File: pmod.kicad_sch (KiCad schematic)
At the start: 2 parts, among them J5 PinSocket_2x6_P2.54mm_Drill1.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, J6 PinSocket_2x6_P2.54mm_Drill1.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

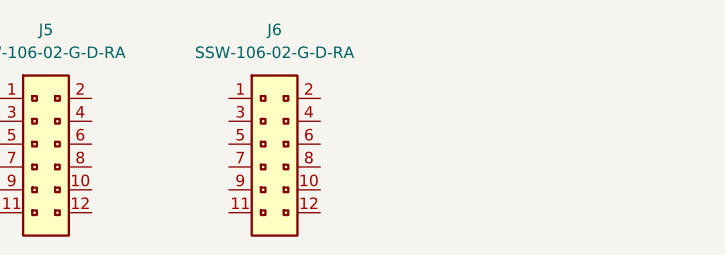
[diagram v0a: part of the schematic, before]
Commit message: [#94684] Add ports to subsheets
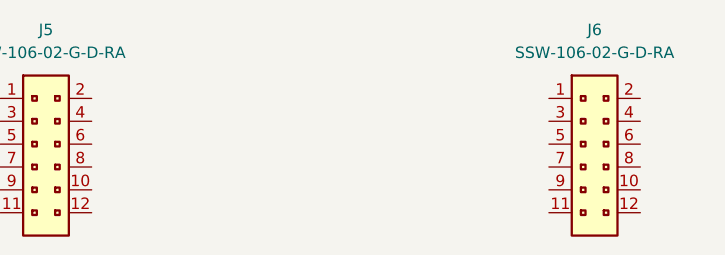
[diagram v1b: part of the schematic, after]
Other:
- moved on the sheet: J6
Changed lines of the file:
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@@
 	(generator "eeschema")
 	(generator_version "9.0")
-	(paper "A4")
+	(paper "A3")
 	(title_block
 		(title "renode-reference-platform")
@@
 	(symbol
 		(lib_id "antmicroGenericPinSockets:PinSocket_2x6_P2.54mm_Drill1.04mm_Horizontal")
-		(at 146.05 86.36 0)
+		(at 181.61 86.36 0)
 		(unit 1)
 		(exclude_from_sim no)
@@
 		(fields_autoplaced yes)
 		(property "Reference" "J6"
-			(at 151.13 78.74 0)
+			(at 186.69 78.74 0)
 			(effects
 				(font
@@
 		)
 		(property "Value" "PinSocket_2x6_P2.54mm_Drill1.04mm_Horizontal"
-			(at 165.1 88.9 0)
+			(at 200.66 88.9 0)
 			(effects
 				(font
@@
 		)
 		(property "Footprint" "antmicro-footprints:PinSocket_2x6_P2.54mm_Drill1.04mm_Horizontal"
-			(at 165.1 91.44 0)
+			(at 200.66 91.44 0)
 			(effects
 				(font
@@
 		)
 		(property "Datasheet" "https://suddendocs.samtec.com/prints/ssw-1xx-xx-xxx-x-xx-xxx-xx-mkt.pdf"
-			(at 165.1 93.98 0)
+			(at 200.66 93.98 0)
 			(effects
 				(font
@@
 		)
 		(property "Description" "PCB Receptacle, Board-to-Board, 2.54 mm, 2 Rows, 12 Contacts, Through Hole Mount Right Angle, SSW"
-			(at 165.1 106.68 0)
+			(at 200.66 106.68 0)
 			(effects
 				(font
@@
 		)
 		(property "MPN" "SSW-106-02-G-D-RA"
-			(at 151.13 81.28 0)
+			(at 186.69 81.28 0)
 			(effects
 				(font
@@
 		)
 		(property "Manufacturer" "Samtec"
-			(at 165.1 96.52 0)
+			(at 200.66 96.52 0)
 			(effects
 				(font
@@
 		)
 		(property "Author" "Antmicro"
-			(at 165.1 101.6 0)
+			(at 200.66 101.6 0)
 			(effects
 				(font
@@
 		)
 		(property "License" "Apache-2.0"
-			(at 165.1 104.14 0)
-			(effects
-				(font
+			(at 200.66 104.14 0)
+			(effects
+				(font

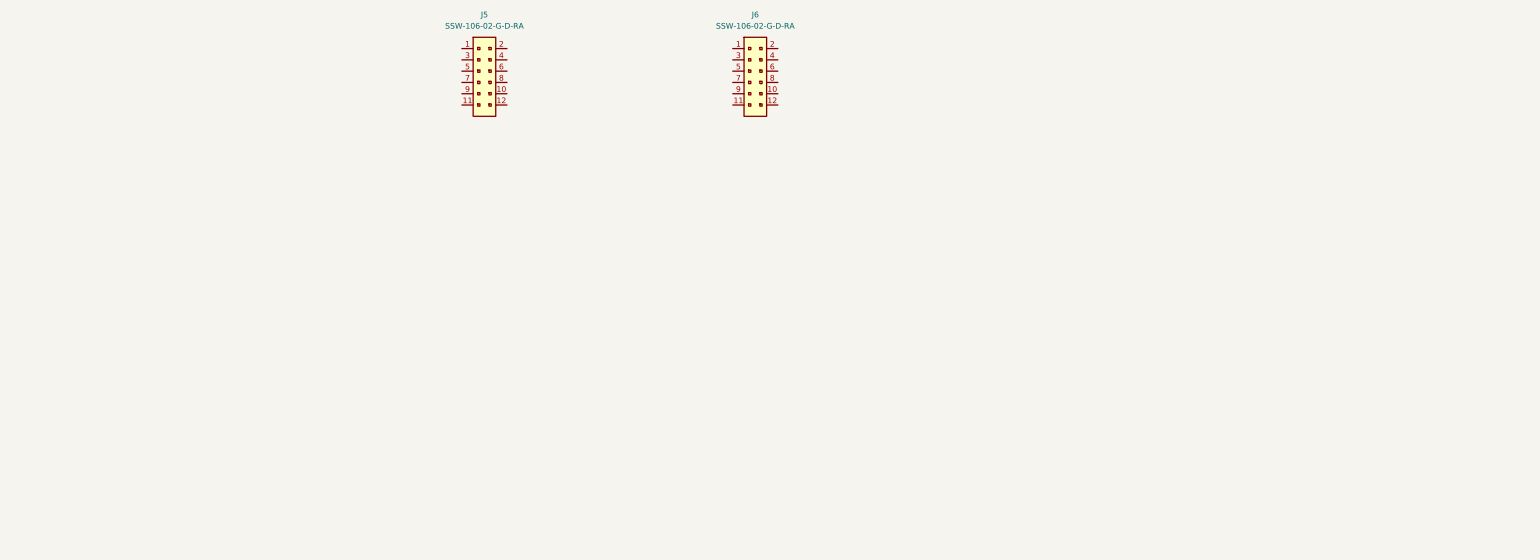
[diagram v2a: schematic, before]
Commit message: [#94862] Add PMOD interfaces
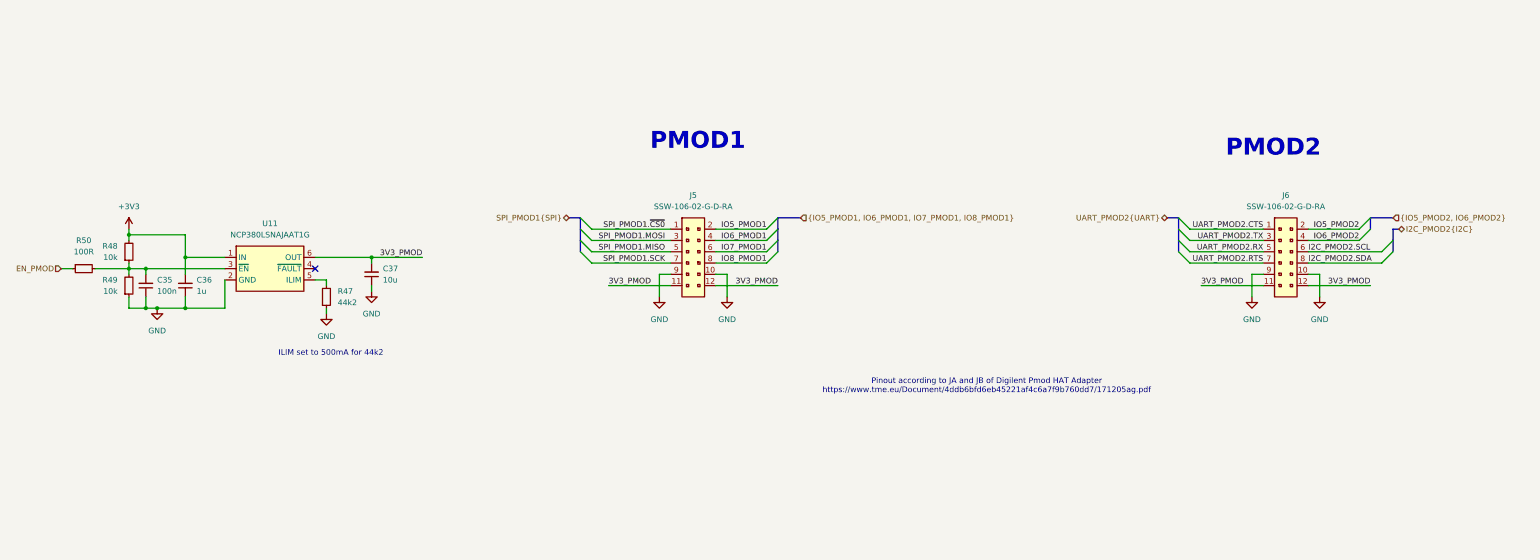
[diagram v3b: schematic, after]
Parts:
- added C35: C_100n_0402, antmicro-footprints:C_0402_1005Metric, symbol antmicroCapacitors0402:C_100n_0402
- added C36: C_1u_0402, antmicro-footprints:C_0402_1005Metric, symbol antmicroCapacitors0402:C_1u_0402
- added C37: C_10u_0402, antmicro-footprints:C_0402_1005Metric, symbol antmicroCapacitors0402:C_10u_0402
- added R47: R_44k2_0402, antmicro-footprints:R_0402_1005Metric, symbol antmicroResistors0402:R_44k2_0402
- added R48, R49: R_10k_0402, antmicro-footprints:R_0402_1005Metric, symbol antmicroResistors0402:R_10k_0402
- added R50: R_100R_0402, antmicro-footprints:R_0402_1005Metric, symbol antmicroResistors0402:R_100R_0402
- added U11: NCP380LSNAJAAT1G, antmicro-footprints:SOT-23-6, symbol antmicroPMICPowerDistributionSwitchesLoadDrivers:NCP380LSNAJAAT1G
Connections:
- net SPI_PMOD1.~{CS0}: now reaches J5.1
- net GND: now reaches J5.10
- net GND: now also J5.9, J6.10, J6.9, C35.1, C36.1, C37.1, R47.1, R49.1, U11.2 (GND)
- net 3V3_PMOD: now reaches J5.11
- net 3V3_PMOD: now also J5.12, J6.11, J6.12, C37.2, U11.6 (OUT)
- net IO5_PMOD1: now reaches J5.2
- net SPI_PMOD1.MOSI: now reaches J5.3
- net IO6_PMOD1: now reaches J5.4
- net SPI_PMOD1.MISO: now reaches J5.5
- net IO7_PMOD1: now reaches J5.6
- net SPI_PMOD1.SCK: now reaches J5.7
- net IO8_PMOD1: now reaches J5.8
- net UART_PMOD2.CTS: now reaches J6.1
- net IO5_PMOD2: now reaches J6.2
- net UART_PMOD2.TX: now reaches J6.3
- net IO6_PMOD2: now reaches J6.4
- net UART_PMOD2.RX: now reaches J6.5
- net I2C_PMOD2.SCL: now reaches J6.6
- net UART_PMOD2.RTS: now reaches J6.7
- net I2C_PMOD2.SDA: now reaches J6.8
- new net: C35.2, R48.1, R49.2, R50.2, U11.3 (~{EN})
- new net: R47.2, U11.5 (ILIM)
- new net +3V3: C36.2, R48.2, U11.1 (IN)
- new net EN_PMOD: R50.1
- no-connect marks 0 -> 1
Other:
- note added: "ILIM set to 500mA for 44k2"
- note added: "PMOD1"
- note added: "PMOD2"
- note added: "Pinout according to JA and JB of Digilent Pmod HAT Adapter https://www.tme.eu/Document/4ddb6bfd6eb45221af4c6a7f9b760dd7/171205ag.pdf"
- moved on the sheet: J5, J6

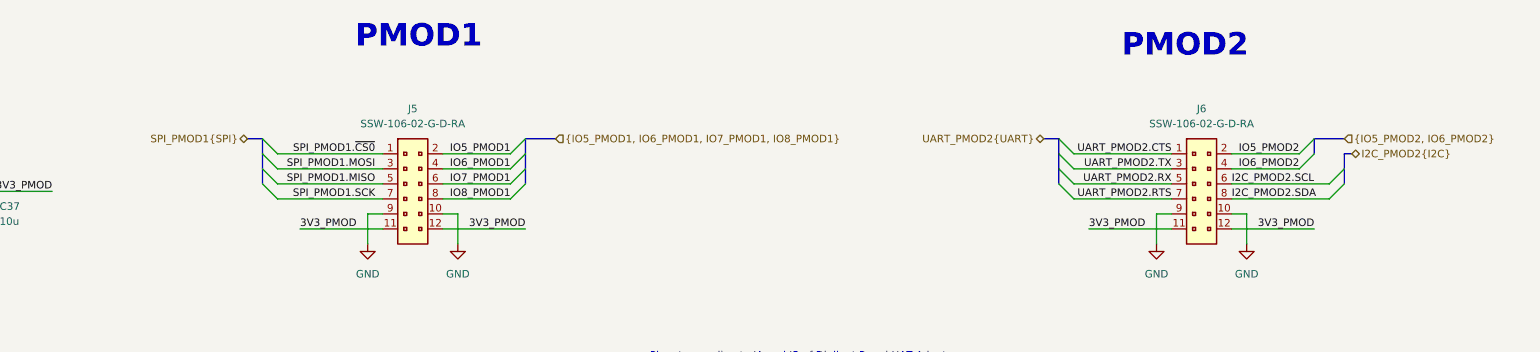
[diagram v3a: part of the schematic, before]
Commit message: [#95036] Rename PMOD signals
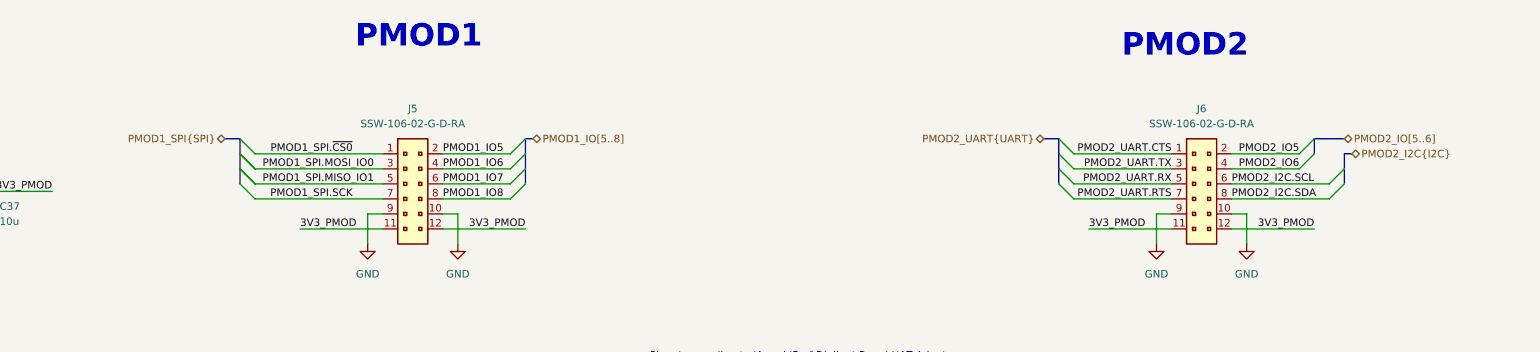
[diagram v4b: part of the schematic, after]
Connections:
- net I2C_PMOD2.SCL renamed PMOD2_I2C.SCL
- net I2C_PMOD2.SDA renamed PMOD2_I2C.SDA
- net IO5_PMOD1 renamed PMOD1_IO5
- net IO5_PMOD2 renamed PMOD2_IO5
- net IO6_PMOD1 renamed PMOD1_IO6
- net IO6_PMOD2 renamed PMOD2_IO6
- net IO7_PMOD1 renamed PMOD1_IO7
- net IO8_PMOD1 renamed PMOD1_IO8
- net SPI_PMOD1.MISO renamed PMOD1_SPI.MISO_IO1
- net SPI_PMOD1.MOSI renamed PMOD1_SPI.MOSI_IO0
- net SPI_PMOD1.SCK renamed PMOD1_SPI.SCK
- net SPI_PMOD1.~{CS0} renamed PMOD1_SPI.~{CS0}
- net UART_PMOD2.CTS renamed PMOD2_UART.CTS
- net UART_PMOD2.RTS renamed PMOD2_UART.RTS
- net UART_PMOD2.RX renamed PMOD2_UART.RX
- net UART_PMOD2.TX renamed PMOD2_UART.TX

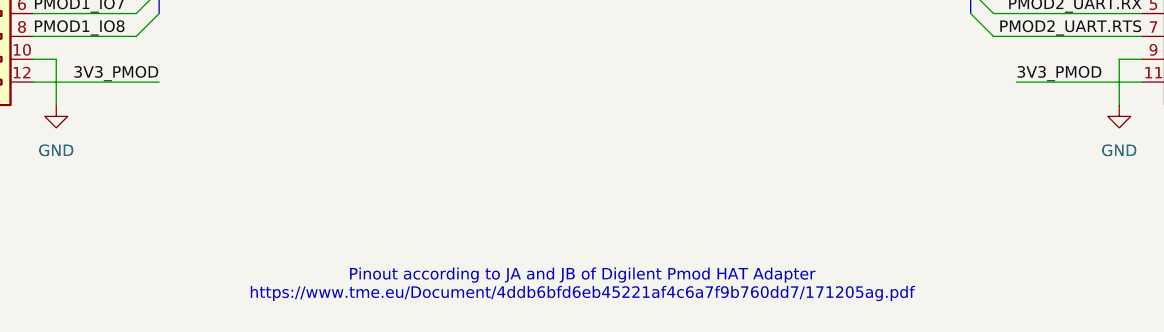
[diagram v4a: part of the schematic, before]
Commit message: [#95036] Connect PMOD pins to MCU
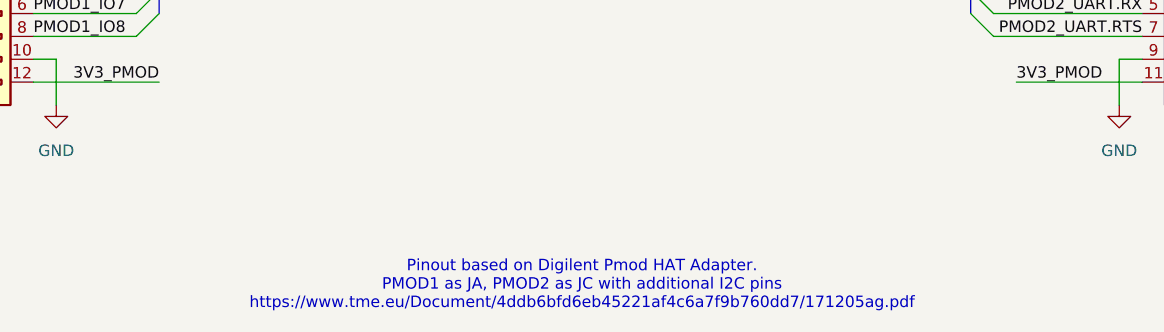
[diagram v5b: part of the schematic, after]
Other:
- note added: "Pinout based on Digilent Pmod HAT Adapter. PMOD1 as JA, PMOD2 as JC with additional I2C pins https://www.tme.eu/Document/4ddb6bfd6eb45221af4c6a7f9b760dd7/171205ag.pdf"
- note removed: "Pinout according to JA and JB of Digilent Pmod HAT Adapter https://www.tme.eu/Document/4ddb6bfd6eb45221af4c6a7f9b760dd7/171205ag.pdf"
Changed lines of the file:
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@@
 		(company "Antmicro")
 	)
-	(text "Pinout according to JA and JB of Digilent Pmod HAT Adapter\nhttps://www.tme.eu/Document/4ddb6bfd6eb45221af4c6a7f9b760dd7/171205ag.pdf"
+	(text "Pinout based on Digilent Pmod HAT Adapter.\nPMOD1 as JA, PMOD2 as JC with additional I2C pins \nhttps://www.tme.eu/Document/4ddb6bfd6eb45221af4c6a7f9b760dd7/171205ag.pdf"
 		(exclude_from_sim no)
 		(at 238.76 162.306 0)

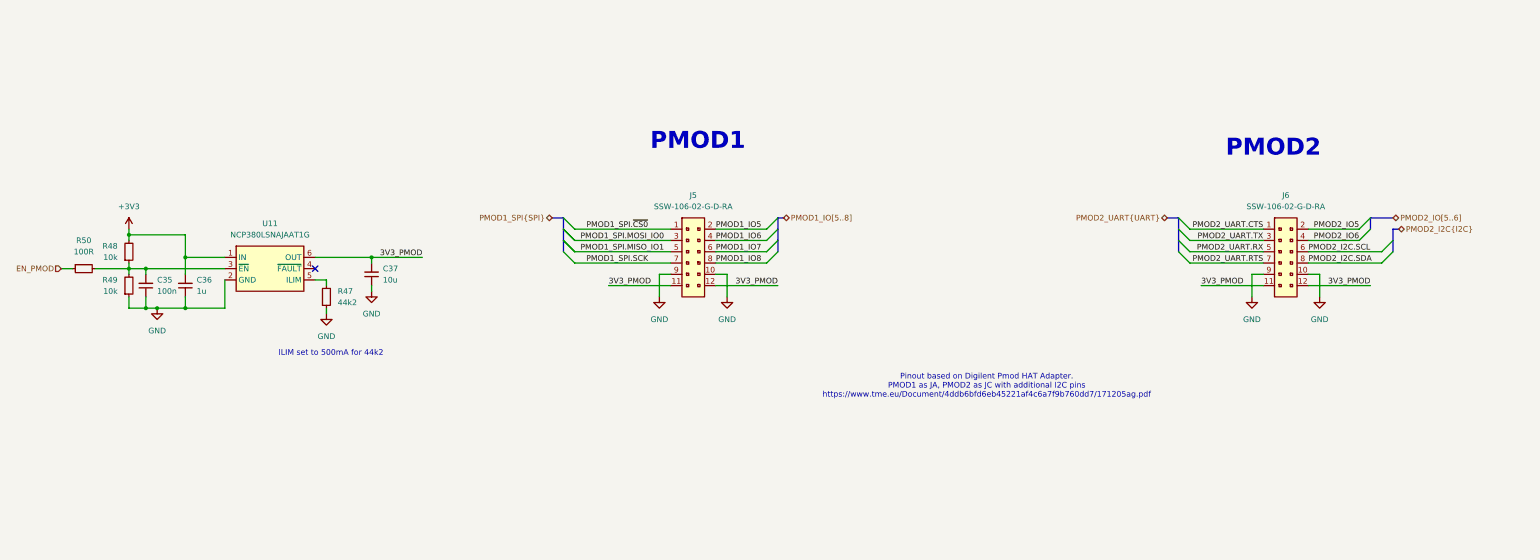
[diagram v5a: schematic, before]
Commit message: [#95036] Add schematic markings
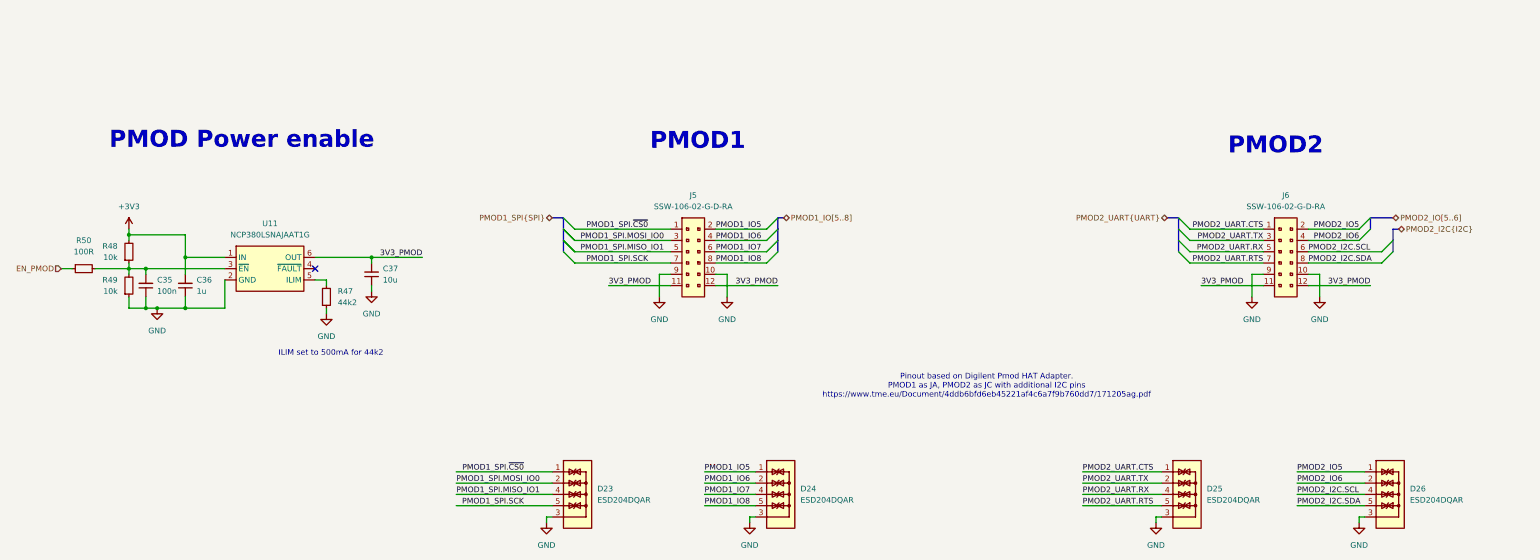
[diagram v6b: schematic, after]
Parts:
- added D23, D24, D25, D26: ESD204DQAR, antmicro-footprints:USON-10_2.5x1mm_P0.5mm, symbol antmicroTVSDiodes:ESD204DQAR
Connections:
- net GND: now also D23.3, D23.8, D24.3, D24.8, D25.3, D25.8, D26.3, D26.8
- net PMOD1_IO5: now also D24.1, D24.10
- net PMOD1_IO6: now also D24.2, D24.9
- net PMOD1_IO7: now also D24.4, D24.7
- net PMOD1_IO8: now also D24.5, D24.6
- net PMOD1_SPI.MISO_IO1: now also D23.4, D23.7
- net PMOD1_SPI.MOSI_IO0: now also D23.2, D23.9
- net PMOD1_SPI.SCK: now also D23.5, D23.6
- net PMOD1_SPI.~{CS0}: now also D23.1, D23.10
- net PMOD2_I2C.SCL: now also D26.4, D26.7
- net PMOD2_I2C.SDA: now also D26.5, D26.6
- net PMOD2_IO5: now also D26.1, D26.10
- net PMOD2_IO6: now also D26.2, D26.9
- net PMOD2_UART.CTS: now also D25.1, D25.10
- net PMOD2_UART.RTS: now also D25.5, D25.6
- net PMOD2_UART.RX: now also D25.4, D25.7
- net PMOD2_UART.TX: now also D25.2, D25.9
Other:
- note added: "PMOD Power enable"

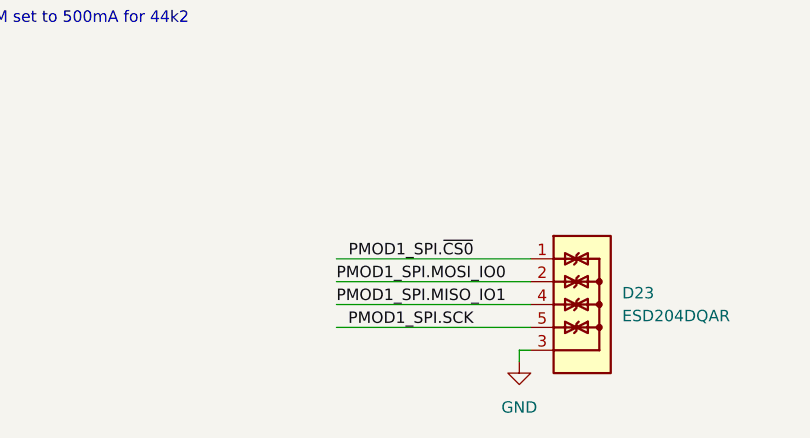
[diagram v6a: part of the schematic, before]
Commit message: [#95036] Solve ERC
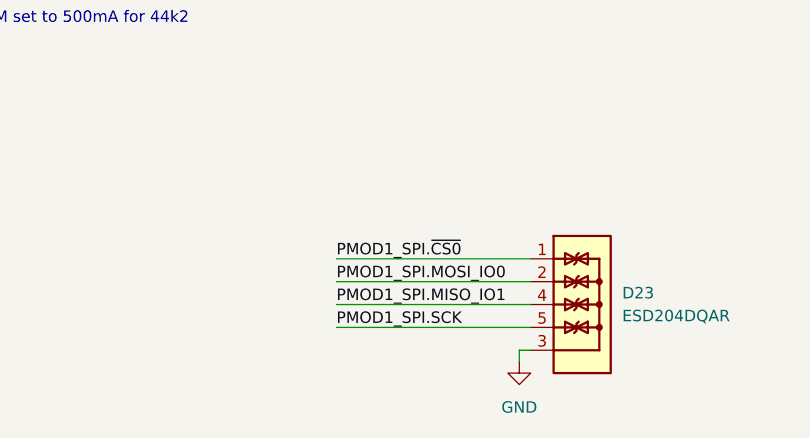
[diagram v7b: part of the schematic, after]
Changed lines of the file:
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@@
 	)
 	(label "PMOD1_SPI.SCK"
-		(at 134.62 189.23 180)
-		(effects
-			(font
-				(size 1.27 1.27)
-			)
-			(justify right bottom)
+		(at 119.38 189.23 0)
+		(effects
+			(font
+				(size 1.27 1.27)
+			)
+			(justify left bottom)
 		)
 	)
@@
 	)
 	(label "PMOD1_SPI.~{CS0}"
-		(at 134.62 181.61 180)
-		(effects
-			(font
-				(size 1.27 1.27)
-			)
-			(justify right bottom)
-		)
-	)
+		(at 119.38 181.61 0)
+		(effects
+			(font
+				(size 1.27 1.27)
+			)
+			(justify left bottom)
+		)
+	)
